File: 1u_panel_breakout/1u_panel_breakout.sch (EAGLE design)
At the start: 6 parts

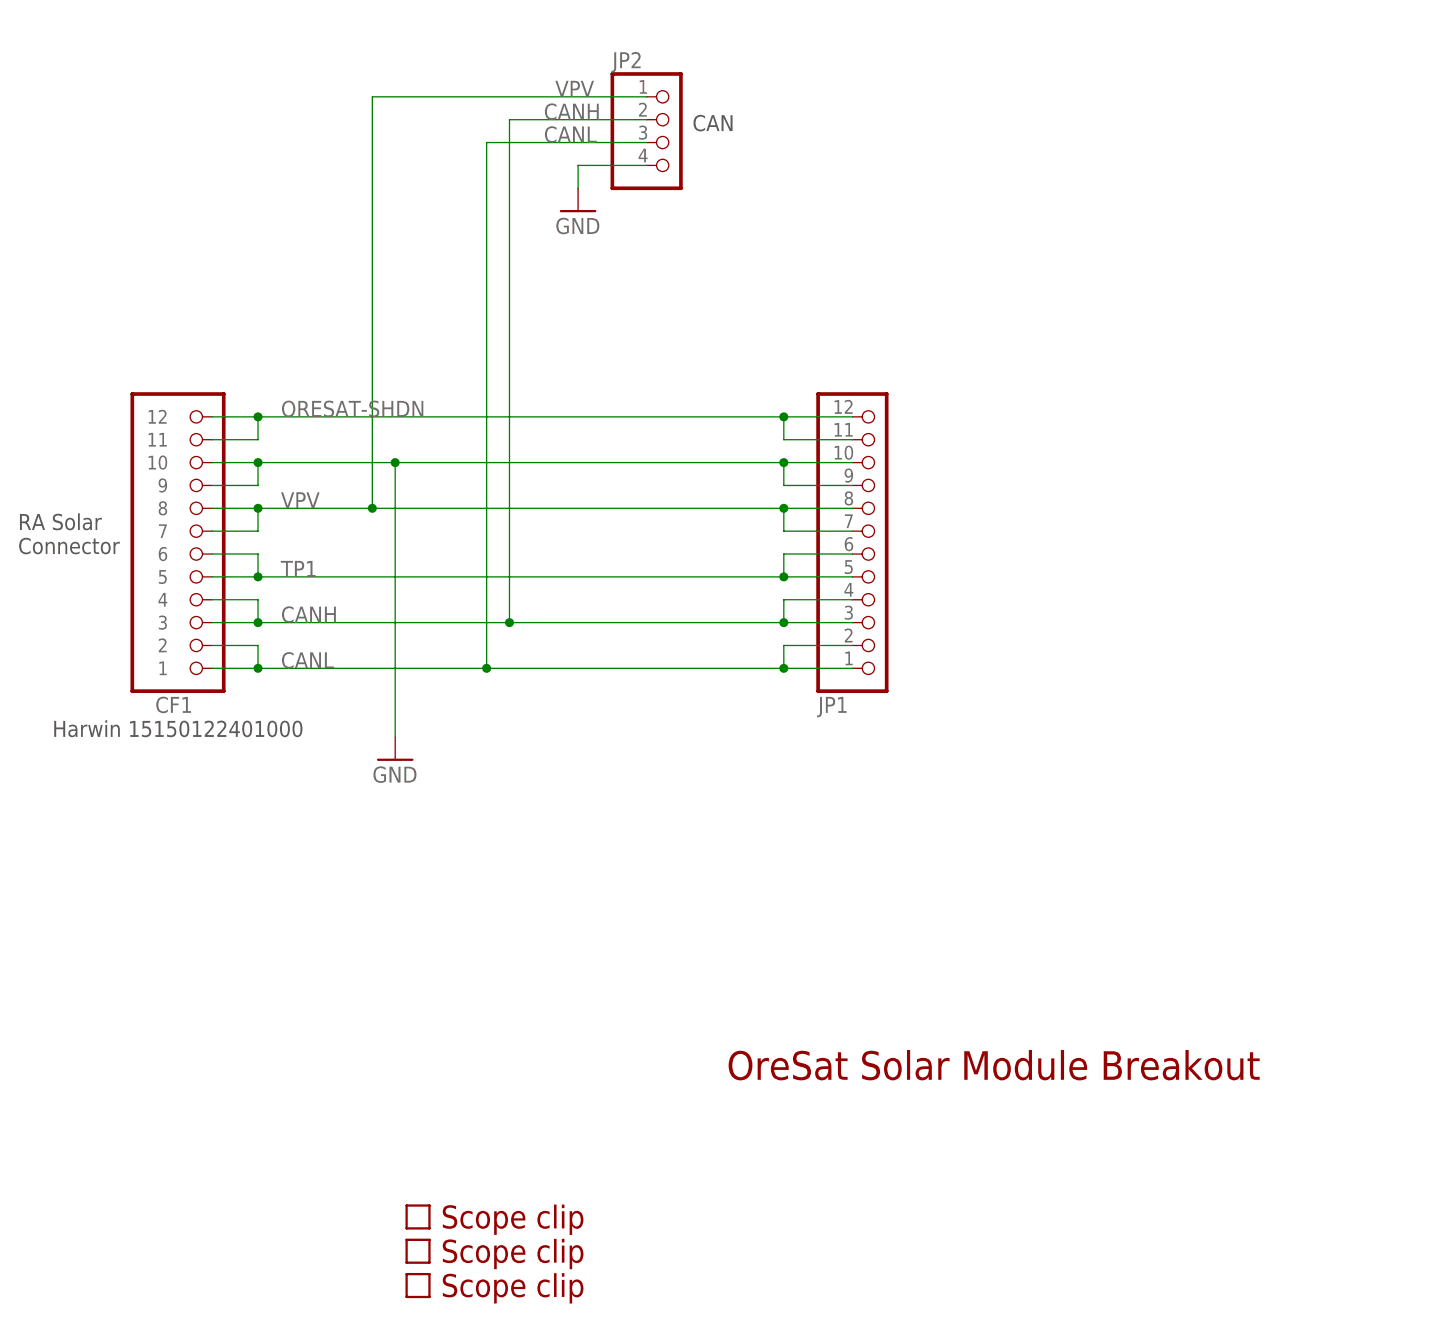
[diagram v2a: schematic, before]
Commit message: Updated solar breakout board (for main connector).
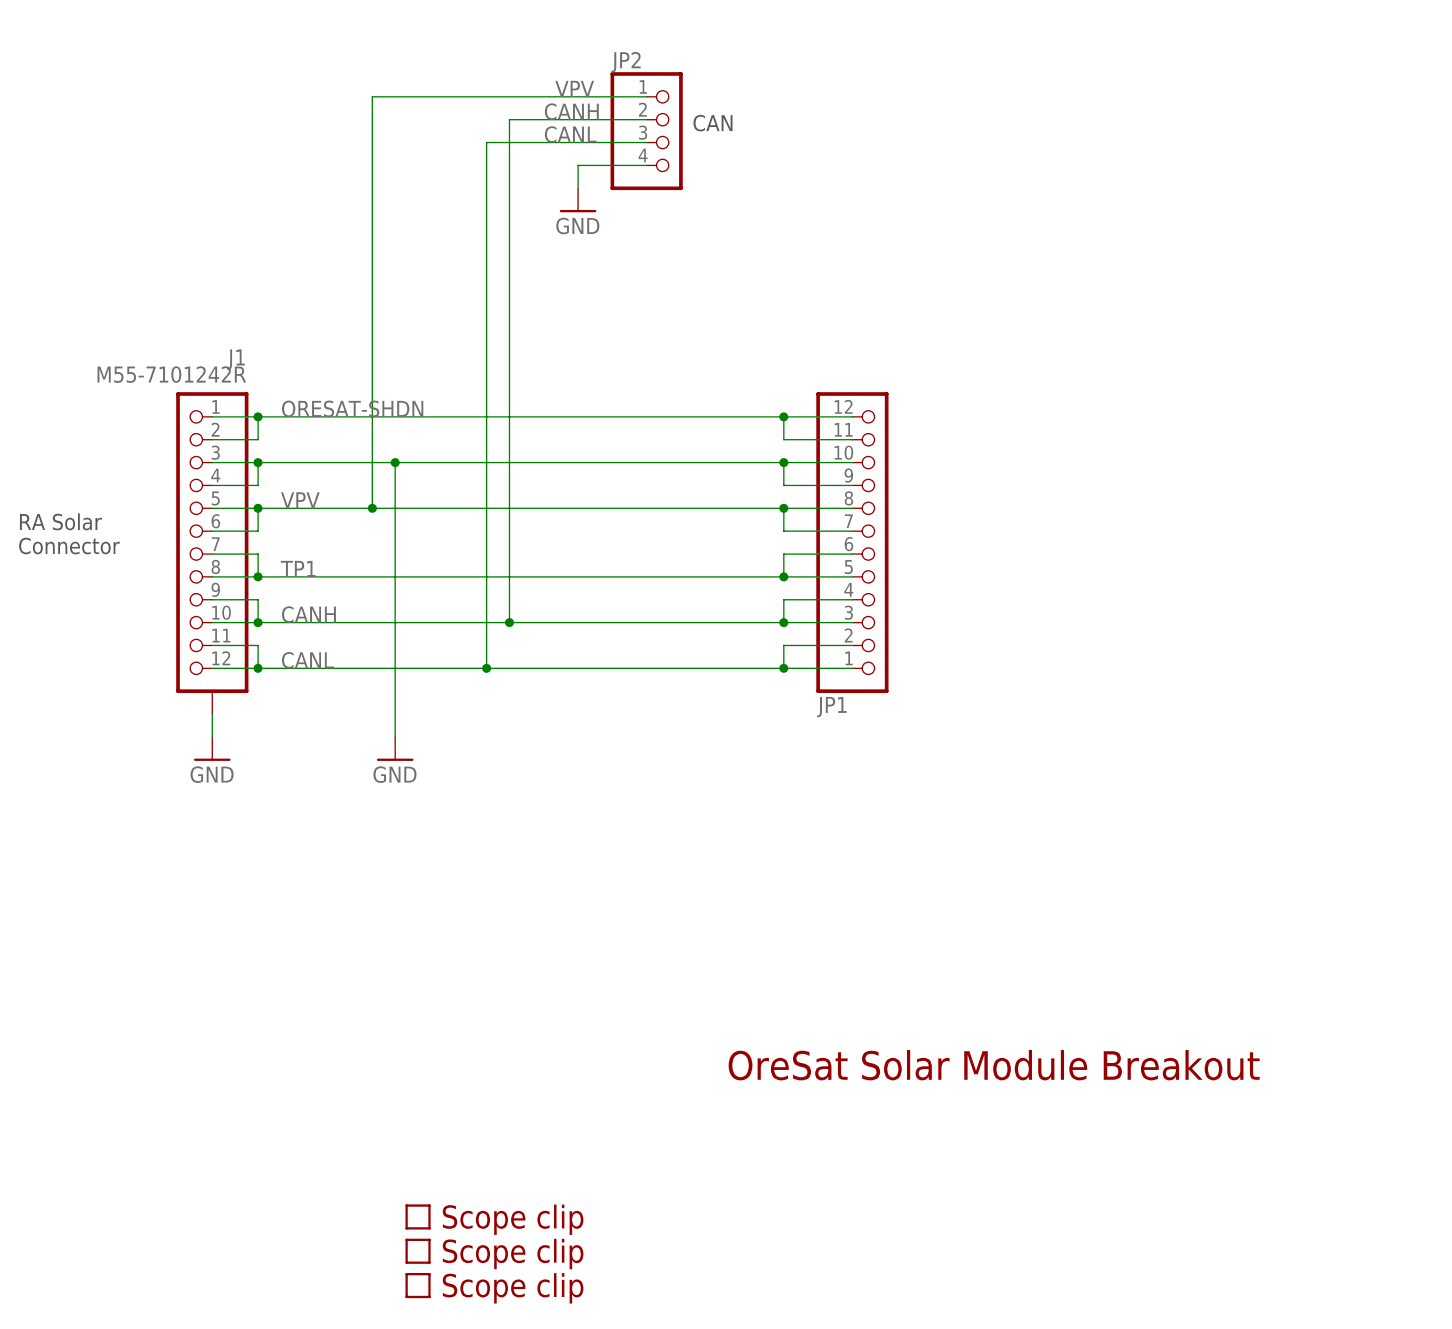
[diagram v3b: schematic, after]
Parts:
- removed CF1: 15150122401000, oresat-connectors:ORESAT-SOLARPANEL-CARD-12PIN
- added J1: M55-7101242R, J-Harwin-M55-7101242-12pin-1.27mm-M-RA:M55-7101242R
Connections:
- net CANH: now also J1.10, J1.9; no longer CF1.3, CF1.4
- net CANL: now also J1.11, J1.12; no longer CF1.1, CF1.2
- net GND: now also J1.3, J1.4, J1.SHIELD; no longer CF1.10, CF1.9
- net ORESAT-SHDN: now also J1.1, J1.2; no longer CF1.11, CF1.12
- net TP1: now also J1.7, J1.8; no longer CF1.5, CF1.6
- net VPV: now also J1.5, J1.6; no longer CF1.7, CF1.8
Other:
- note removed: "Harwin 15150122401000"
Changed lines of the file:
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@@
 <?xml version="1.0" encoding="utf-8"?>
 <!DOCTYPE eagle SYSTEM "eagle.dtd">
-<eagle version="8.6.0">
+<eagle version="9.3.2">
 <drawing>
 <settings>
@@
 <layer number="59" name="tCarbon" color="7" fill="1" visible="no" active="no"/>
 <layer number="60" name="bCarbon" color="7" fill="1" visible="no" active="no"/>
+<layer number="88" name="SimResults" color="9" fill="1" visible="yes" active="yes"/>
+<layer number="89" name="SimProbes" color="9" fill="1" visible="yes" active="yes"/>
 <layer number="90" name="Modules" color="5" fill="1" visible="yes" active="yes"/>
 <layer number="91" name="Nets" color="2" fill="1" visible="yes" active="yes"/>
@@
 <parts>
 <part name="FRAME1" library="frames" deviceset="LETTER_L" device=""/>
-<part name="CF1" library="oresat-connectors" deviceset="ORESAT-SOLARPANEL-CARD-12PIN" device="" value="15150122401000"/>
 <part name="JP1" library="pinhead" deviceset="PINHD-1X12" device=""/>
 <part name="GND1" library="supply1" deviceset="GND" device=""/>
@@
 <part name="U$2" library="oresat-misc" deviceset="SCOPE_CLIP" device=""/>
 <part name="U$3" library="oresat-misc" deviceset="SCOPE_CLIP" device=""/>
+<part name="J1" library="J-Harwin-M55-7101242-12pin-1.27mm-M-RA" deviceset="M55-7101242R" device=""/>
+<part name="GND3" library="supply1" deviceset="GND" device=""/>
 </parts>
 <sheets>
@@
 Connector</text>
 <text x="111.76" y="85.09" size="1.778" layer="97">CAN</text>
-<text x="40.64" y="17.78" size="1.778" layer="97">Harwin 15150122401000</text>
 </plain>
 <instances>
-<instance part="FRAME1" gate="G$1" x="-35.56" y="-48.26"/>
-<instance part="FRAME1" gate="G$2" x="111.76" y="-48.26"/>
-<instance part="CF1" gate="G$1" x="58.42" y="39.37" rot="MR180"/>
-<instance part="JP1" gate="G$1" x="132.08" y="38.1" rot="MR180"/>
-<instance part="GND1" gate="1" x="78.74" y="15.24"/>
-<instance part="GND2" gate="1" x="99.06" y="76.2"/>
-<instance part="JP2" gate="A" x="109.22" y="83.82"/>
-<instance part="U$1" gate="G$1" x="81.28" y="-43.18"/>
-<instance part="U$2" gate="G$1" x="81.28" y="-39.37"/>
-<instance part="U$3" gate="G$1" x="81.28" y="-35.56"/>
+<instance part="FRAME1" gate="G$1" x="-35.56" y="-48.26" smashed="yes"/>
+<instance part="FRAME1" gate="G$2" x="111.76" y="-48.26" smashed="yes">
+<attribute name="LAST_DATE_TIME" x="124.46" y="-46.99" size="2.54" layer="94"/>
+<attribute name="SHEET" x="198.12" y="-46.99" size="2.54" layer="94"/>
+<attribute name="DRAWING_NAME" x="129.54" y="-29.21" size="2.54" layer="94"/>
+</instance>
+<instance part="JP1" gate="G$1" x="132.08" y="38.1" smashed="yes" rot="MR180">
+<attribute name="NAME" x="125.73" y="22.225" size="1.778" layer="95" rot="MR180"/>
+<attribute name="VALUE" x="125.73" y="58.42" size="1.778" layer="96" rot="MR180"/>
+</instance>
+<instance part="GND1" gate="1" x="78.74" y="15.24" smashed="yes">
+<attribute name="VALUE" x="76.2" y="12.7" size="1.778" layer="96"/>
+</instance>
+<instance part="GND2" gate="1" x="99.06" y="76.2" smashed="yes">
+<attribute name="VALUE" x="96.52" y="73.66" size="1.778" layer="96"/>
+</instance>
+<instance part="JP2" gate="A" x="109.22" y="83.82" smashed="yes">
+<attribute name="NAME" x="102.87" y="92.075" size="1.778" layer="95"/>
+<attribute name="VALUE" x="102.87" y="76.2" size="1.778" layer="96"/>
+</instance>
+<instance part="U$1" gate="G$1" x="81.28" y="-43.18" smashed="yes"/>
+<instance part="U$2" gate="G$1" x="81.28" y="-39.37" smashed="yes"/>
+<instance part="U$3" gate="G$1" x="81.28" y="-35.56" smashed="yes"/>
+<instance part="J1" gate="G$1" x="55.88" y="40.64" smashed="yes" rot="MR0">
+<attribute name="NAME" x="62.23" y="59.055" size="1.778" layer="95" rot="MR0"/>
+<attribute name="VALUE" x="62.23" y="57.15" size="1.778" layer="96" rot="MR0"/>
+</instance>
+<instance part="GND3" gate="1" x="58.42" y="15.24" smashed="yes">
+<attribute name="VALUE" x="55.88" y="12.7" size="1.778" layer="96"/>
+</instance>
 </instances>
 <busses>
@@
 <net name="ORESAT-SHDN" class="0">
 <segment>
-<pinref part="CF1" gate="G$1" pin="12"/>
 <pinref part="JP1" gate="G$1" pin="12"/>
 <wire x1="58.42" y1="53.34" x2="63.5" y2="53.34" width="0.1524" layer="91"/>
@@
 <wire x1="121.92" y1="50.8" x2="121.92" y2="53.34" width="0.1524" layer="91"/>
 <junction x="121.92" y="53.34"/>
-<pinref part="CF1" gate="G$1" pin="11"/>
 <wire x1="58.42" y1="50.8" x2="63.5" y2="50.8" width="0.1524" layer="91"/>
 <wire x1="63.5" y1="50.8" x2="63.5" y2="53.34" width="0.1524" layer="91"/>
 <junction x="63.5" y="53.34"/>
 <label x="66.04" y="53.34" size="1.778" layer="95"/>
+<pinref part="J1" gate="G$1" pin="1"/>
+<pinref part="J1" gate="G$1" pin="2"/>
 </segment>
 </net>
 <net name="CANL" class="0">
 <segment>
-<pinref part="CF1" gate="G$1" pin="1"/>
 <pinref part="JP1" gate="G$1" pin="1"/>
 <wire x1="58.42" y1="25.4" x2="63.5" y2="25.4" width="0.1524" layer="91"/>
@@
 <wire x1="121.92" y1="27.94" x2="121.92" y2="25.4" width="0.1524" layer="91"/>
 <junction x="121.92" y="25.4"/>
-<pinref part="CF1" gate="G$1" pin="2"/>
 <wire x1="58.42" y1="27.94" x2="63.5" y2="27.94" width="0.1524" layer="91"/>
 <wire x1="63.5" y1="27.94" x2="63.5" y2="25.4" width="0.1524" layer="91"/>
@@
 <wire x1="106.68" y1="83.82" x2="88.9" y2="83.82" width="0.1524" layer="91"/>
 <label x="95.25" y="83.82" size="1.778" layer="95"/>
+<pinref part="J1" gate="G$1" pin="11"/>
+<pinref part="J1" gate="G$1" pin="12"/>
 </segment>
 </net>
 <net name="CANH" class="0">
 <segment>
-<pinref part="CF1" gate="G$1" pin="3"/>
 <pinref part="JP1" gate="G$1" pin="3"/>
 <wire x1="58.42" y1="30.48" x2="63.5" y2="30.48" width="0.1524" layer="91"/>
@@
 <wire x1="121.92" y1="33.02" x2="121.92" y2="30.48" width="0.1524" layer="91"/>
 <junction x="121.92" y="30.48"/>
-<pinref part="CF1" gate="G$1" pin="4"/>
 <wire x1="58.42" y1="33.02" x2="63.5" y2="33.02" width="0.1524" layer="91"/>
 <wire x1="63.5" y1="33.02" x2="63.5" y2="30.48" width="0.1524" layer="91"/>
@@
 <wire x1="91.44" y1="86.36" x2="106.68" y2="86.36" width="0.1524" layer="91"/>
 <label x="95.25" y="86.36" size="1.778" layer="95"/>
+<pinref part="J1" gate="G$1" pin="9"/>
+<pinref part="J1" gate="G$1" pin="10"/>
 </segment>
 </net>
 <net name="VPV" class="0">
 <segment>
-<pinref part="CF1" gate="G$1" pin="8"/>
 <pinref part="JP1" gate="G$1" pin="8"/>
 <wire x1="58.42" y1="43.18" x2="63.5" y2="43.18" width="0.1524" layer="91"/>
@@
 <wire x1="121.92" y1="40.64" x2="121.92" y2="43.18" width="0.1524" layer="91"/>
 <junction x="121.92" y="43.18"/>
-<pinref part="CF1" gate="G$1" pin="7"/>
 <wire x1="58.42" y1="40.64" x2="63.5" y2="40.64" width="0.1524" layer="91"/>
 <wire x1="63.5" y1="40.64" x2="63.5" y2="43.18" width="0.1524" layer="91"/>
@@
 <wire x1="76.2" y1="88.9" x2="106.68" y2="88.9" width="0.1524" layer="91"/>
 <label x="96.52" y="88.9" size="1.778" layer="95"/>
+<pinref part="J1" gate="G$1" pin="5"/>
+<pinref part="J1" gate="G$1" pin="6"/>
 </segment>
 </net>
@@
 <segment>
 <pinref part="JP1" gate="G$1" pin="5"/>
-<pinref part="CF1" gate="G$1" pin="5"/>
 <wire x1="129.54" y1="35.56" x2="121.92" y2="35.56" width="0.1524" layer="91"/>
-<pinref part="CF1" gate="G$1" pin="6"/>
 <pinref part="JP1" gate="G$1" pin="6"/>
 <wire x1="63.5" y1="35.56" x2="58.42" y2="35.56" width="0.1524" layer="91"/>
@@
 <junction x="63.5" y="35.56"/>
 <junction x="121.92" y="35.56"/>
+<pinref part="J1" gate="G$1" pin="7"/>
+<pinref part="J1" gate="G$1" pin="8"/>
 </segment>
 </net>
 <net name="GND" class="0">
 <segment>
-<pinref part="CF1" gate="G$1" pin="10"/>
 <pinref part="JP1" gate="G$1" pin="10"/>
 <wire x1="58.42" y1="48.26" x2="63.5" y2="48.26" width="0.1524" layer="91"/>
@@
 <wire x1="121.92" y1="45.72" x2="121.92" y2="48.26" width="0.1524" layer="91"/>
 <junction x="121.92" y="48.26"/>
-<pinref part="CF1" gate="G$1" pin="9"/>
 <wire x1="58.42" y1="45.72" x2="63.5" y2="45.72" width="0.1524" layer="91"/>
 <wire x1="63.5" y1="45.72" x2="63.5" y2="48.26" width="0.1524" layer="91"/>
@@
 <wire x1="78.74" y1="17.78" x2="78.74" y2="48.26" width="0.1524" layer="91"/>
 <junction x="78.74" y="48.26"/>
+<pinref part="J1" gate="G$1" pin="3"/>
+<pinref part="J1" gate="G$1" pin="4"/>
 </segment>
 <segment>
@@
 <wire x1="99.06" y1="81.28" x2="106.68" y2="81.28" width="0.1524" layer="91"/>
 </segment>
-</net>
+<segment>
+<pinref part="GND3" gate="1" pin="GND"/>
+<pinref part="J1" gate="G$1" pin="SHIELD"/>
+<wire x1="58.42" y1="17.78" x2="58.42" y2="20.32" width="0.1524" layer="91"/>
+</segment>
+</net>
